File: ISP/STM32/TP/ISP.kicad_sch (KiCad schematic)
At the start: 4 parts

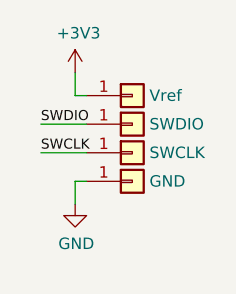
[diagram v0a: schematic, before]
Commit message: Fix grid alignment and update to KiCad 9
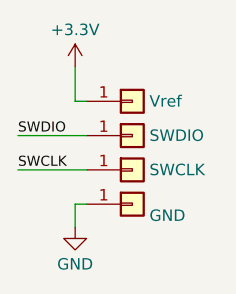
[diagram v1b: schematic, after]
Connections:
- net +3V3 renamed +3.3V
